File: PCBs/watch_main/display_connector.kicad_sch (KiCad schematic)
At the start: 0 parts

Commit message: More PCB progress
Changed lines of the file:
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@@
+    (effects (font (size 1.27 1.27)) (justify left))
+  )
+  (hierarchical_label "PCD" (shape output) (at 243.84 86.36 0) (fields_autoplaced)
     (effects (font (size 1.27 1.27)) (justify left))
   )
@@
     )
   )
-  (hierarchical_label "+4V6" (shape input) (at 243.84 88.9 0) (fields_autoplaced)
+  (hierarchical_label "+4V6" (shape input) (at 243.84 93.98 0) (fields_autoplaced)
     (effects (font (size 1.27 1.27)) (justify left))
   )
-  (hierarchical_label "-2V2" (shape input) (at 243.84 91.44 0) (fields_autoplaced)
+  (hierarchical_label "RESET" (shape input) (at 243.84 83.82 0) (fields_autoplaced)
     (effects (font (size 1.27 1.27)) (justify left))
   )
+  (hierarchical_label "-2V2" (shape input) (at 243.84 96.52 0) (fields_autoplaced)
+    (effects (font (size 1.27 1.27)) (justify left))
+  )
+  (hierarchical_label "DSI_TE" (shape output) (at 243.84 78.74 0) (fields_autoplaced)
+    (effects (font (size 1.27 1.27)) (justify left))
+  )

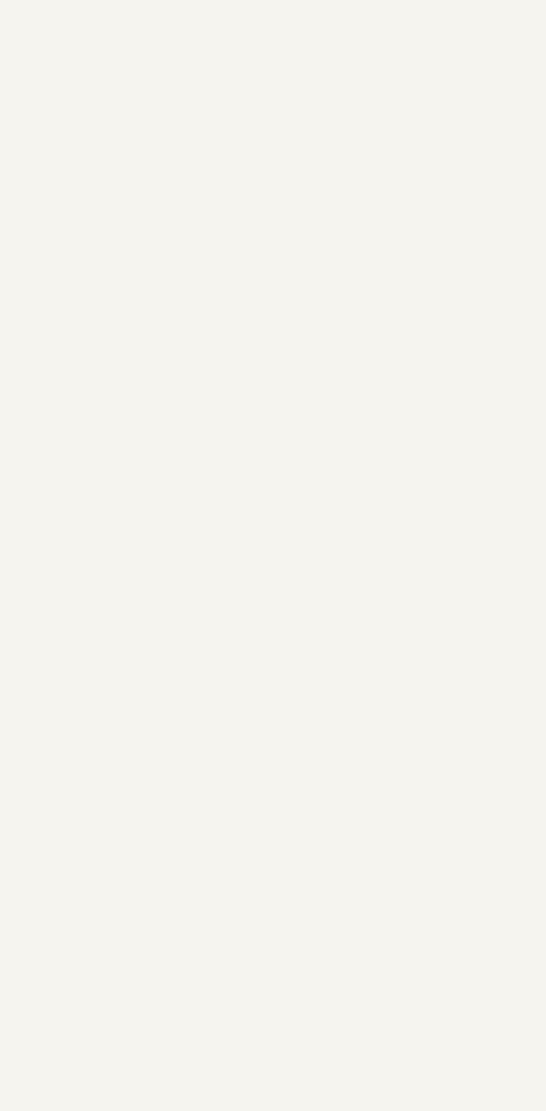
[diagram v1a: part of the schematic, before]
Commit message: Added connector symbols and footprints
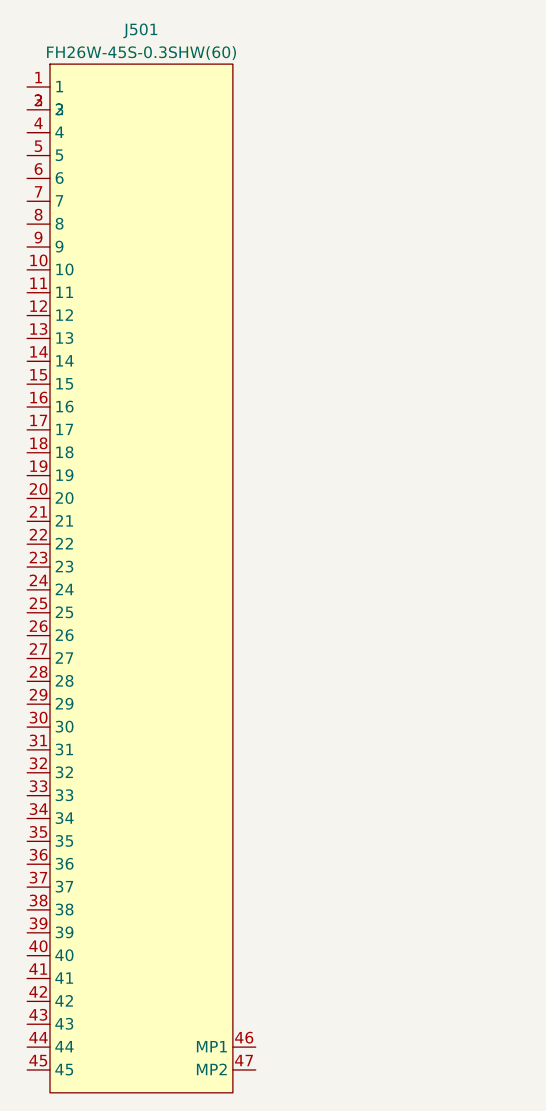
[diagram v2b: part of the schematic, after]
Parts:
- added J501: FH26W-45S-0.3SHW(60), watch_footprints:FH26W-45S-0.3SHW(60), symbol watch_symbols_lib:FH26W-45S-0.3SHW(60)
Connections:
- new net: J501.2, J501.3
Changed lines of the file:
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@@
     (effects (font (size 1.27 1.27)) (justify left))
   )
+  (symbol (lib_id "watch_symbols_lib:FH26W-45S-0.3SHW(60)") (at 165.1 40.64 0) (unit 1)
+    (in_bom yes) (on_board yes) (dnp no) (fields_autoplaced)
+    (property "Reference" "J501" (at 165.1 36.83 0)
+      (effects (font (size 1.27 1.27)))
+    )
+    (property "Value" "FH26W-45S-0.3SHW(60)" (at 165.1 39.37 0)
+      (effects (font (size 1.27 1.27)))
+    )
+    (property "Footprint" "watch_footprints:FH26W-45S-0.3SHW(60)" (at 165.1 33.02 0)
+      (effects (font (size 1.27 1.27)) hide)
+    )
+    (property "Datasheet" "https://www.mouser.co.uk/datasheet/2/185/FH26W_45S_0_3SHW_60__CL0580_2414_3_60_2DDrawing_00-1614924.pdf" (at 165.1 160.02 0)
+      (effects (font (size 1.27 1.27)) hide)
+    )
+    (pin "1")
+    (pin "10")
+    (pin "11")
+    (pin "12")
+    (pin "13")
+    (pin "14")
+    (pin "15")
+    (pin "16")
+    (pin "17")
+    (pin "18")
+    (pin "19")
+    (pin "2")
+    (pin "20")
+    (pin "21")
+    (pin "22")
+    (pin "23")
+    (pin "24")
+    (pin "25")
+    (pin "26")
+    (pin "27")
+    (pin "28")
+    (pin "29")
+    (pin "3")
+    (pin "30")
+    (pin "31")
+    (pin "32")
+    (pin "33")
+    (pin "34")
+    (pin "35")
+    (pin "36")
+    (pin "37")
+    (pin "38")
+    (pin "39")
+    (pin "4")
+    (pin "40")
+    (pin "41")
+    (pin "42")
+    (pin "43")
+    (pin "44")
+    (pin "45")
+    (pin "46")
+    (pin "47")
+    (pin "5")
+    (pin "6")
+    (pin "7")
+    (pin "8")
+    (pin "9")
+    (instances
+      (project "watch_main"
+        (path "/b008648a-c7cf-4e14-8a0a-b9314d757b4a/e6589a80-c4f6-4562-bcb4-1d61b94d1497"
+          (reference "J501") (unit 1)
+        )
+      )
+    )
+  )
 )

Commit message: Main PCB schematic almost complete
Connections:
- net +4V6: now also J501.37, J501.38, J501.39
- net -2V2: now also J501.41, J501.42, J501.43
- net DSI.CKN: now also J501.20
- net DSI.CKP: now also J501.19
- net DSI.D0N: now also J501.17
- net DSI.D0P: now also J501.16
- net DSI.D1N: now also J501.23
- net DSI.D1P: now also J501.22
- net DSI_TE: now also J501.11
- net OLED_EN: now also J501.29
- net PCD: now also J501.31
- net RESET: now also J501.28
- net GND: now reaches J501.12
- net GND: now also J501.15, J501.18, J501.21, J501.24, J501.27, J501.34, J501.36, J501.40, J501.44, J501.45, J501.9
- net at J501.2: no longer J501.3
- net +3V3: now reaches J501.32
- net +1V8: now reaches J501.33
- no-connect marks 0 -> 17
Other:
- note added: "A1D3T-001"

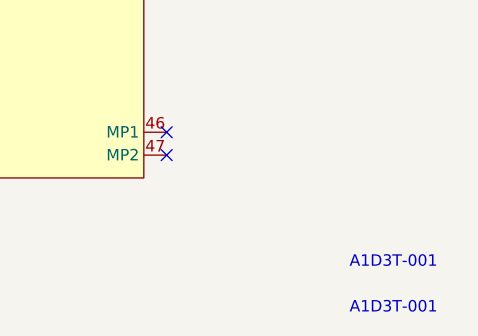
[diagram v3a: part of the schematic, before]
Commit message: Schematic finished and BOM started
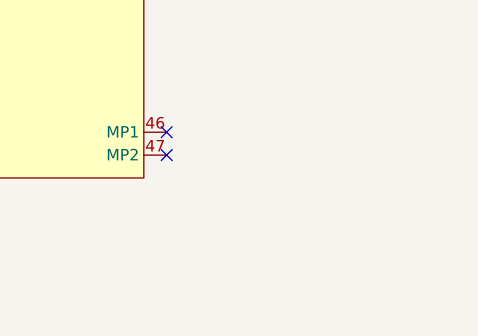
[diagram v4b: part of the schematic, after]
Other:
- note removed: "A1D3T-001"
- title: (none) -> Watch Display Connector
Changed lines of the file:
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@@
 (kicad_sch (version 20230121) (generator eeschema)
   (paper "A4")
+  (title_block
+    (title "Watch Display Connector")
+    (date "2023-12-21")
+    (rev "1")
+    (comment 1 "Checked by Ben Smith on 21/12/23")
+  )
   (junction (at 124.46 137.16) (diameter 0) (color 0 0 0 0)
   )
@@
     )
   )
-  (text "A1D3T-001" (at 180.34 167.64 0)
-    (effects (font (size 1.27 1.27)) (justify left bottom) (href "file://C:\\Users\\bens1\\Documents\\Other\\Projects\\Smart-Watch\\Documentation\\Datasheets/A1D3T-001.pdf"))
-  )
-  (text "A1D3T-001" (at 180.34 172.72 0)
-    (effects (font (size 1.27 1.27)) (justify left bottom) (href "file://${KIPRJMOD}/../../Documentation/Datasheets/A1D3T-001.pdf"))
-  )
   (label "PCD" (at 121.92 119.38 0) (fields_autoplaced)
